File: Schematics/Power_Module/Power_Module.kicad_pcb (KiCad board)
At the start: 4 copper layers, 69.5 x 60 mm, 50 parts, among them J1 ScrewSwitch A, J2 ScrewSwitch B, J3 Battery B, J5 Battery A, J6 Stack Male Edge Connector, Q1 AO4447A, Q2 AO4447A, U1 LMR51430XDDCR, U2 LMR51430XDDCR, U3 LMR51430XDDCR

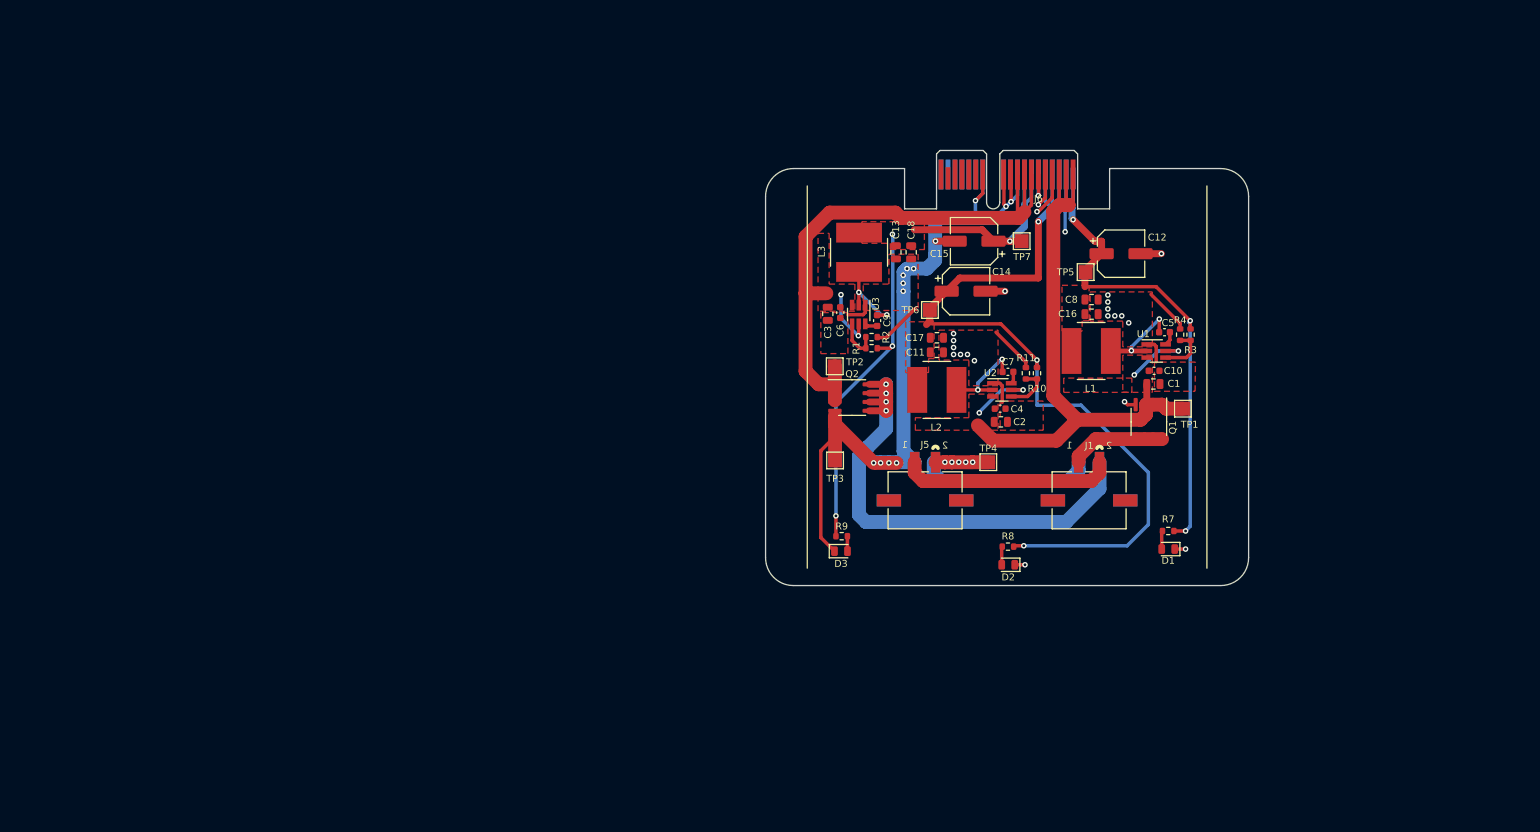
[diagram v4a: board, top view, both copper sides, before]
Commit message: Added part numbers, finalized PCB layout
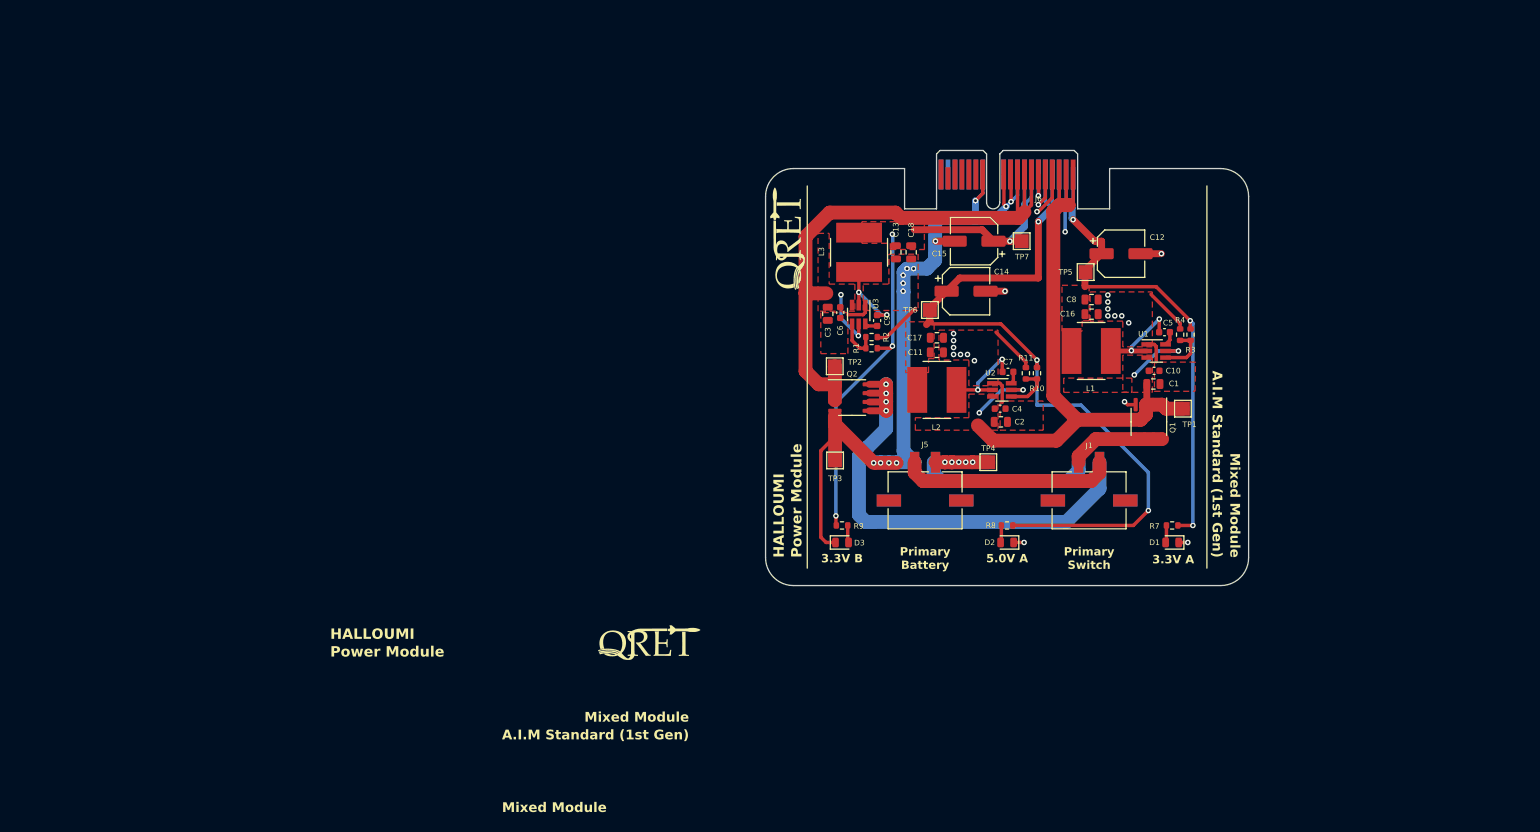
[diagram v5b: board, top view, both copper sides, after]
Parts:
- moved D2 3.21 mm to (165.0, 93.5)
- moved R8 3.05 mm to (165.0, 91.1)
- moved R9 1.55 mm to (141.2, 91.1)
- moved D3 1.26 mm to (141.2, 93.5)
- moved D1 1.11 mm to (188.8, 93.5)
- moved R7 0.98 mm to (188.8, 91.1)
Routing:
- net 5.0V_A: track 114.1 -> 111.8 mm
- net 3.3V_B: track 80.1 -> 78.5 mm
- net GND2: track 127.8 -> 129.0 mm
- net 3.3V_A: track 75.0 -> 74.2 mm
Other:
- board text added: "3.3V A"
- board text added: "3.3V B"
- board text added: "5.0V A"
- board text added: "A.I.M Standard (1st Gen)"
- board text added: "HALLOUMI"
- board text added: "Halloumi Rev 1.0 QRET Mar 2024 Rajan Laird Kennan Bays Oak Campbell"
- board text added: "Mixed Module"
- board text added: "Power Module"
- board text added: "Primary Battery"
- board text added: "Primary Switch"
- board text added: "Secondary Battery"
- board text added: "Secondary Switch"
- board text removed: "PLACE POWER CONNECTORS HERE (okay if on bottom)"

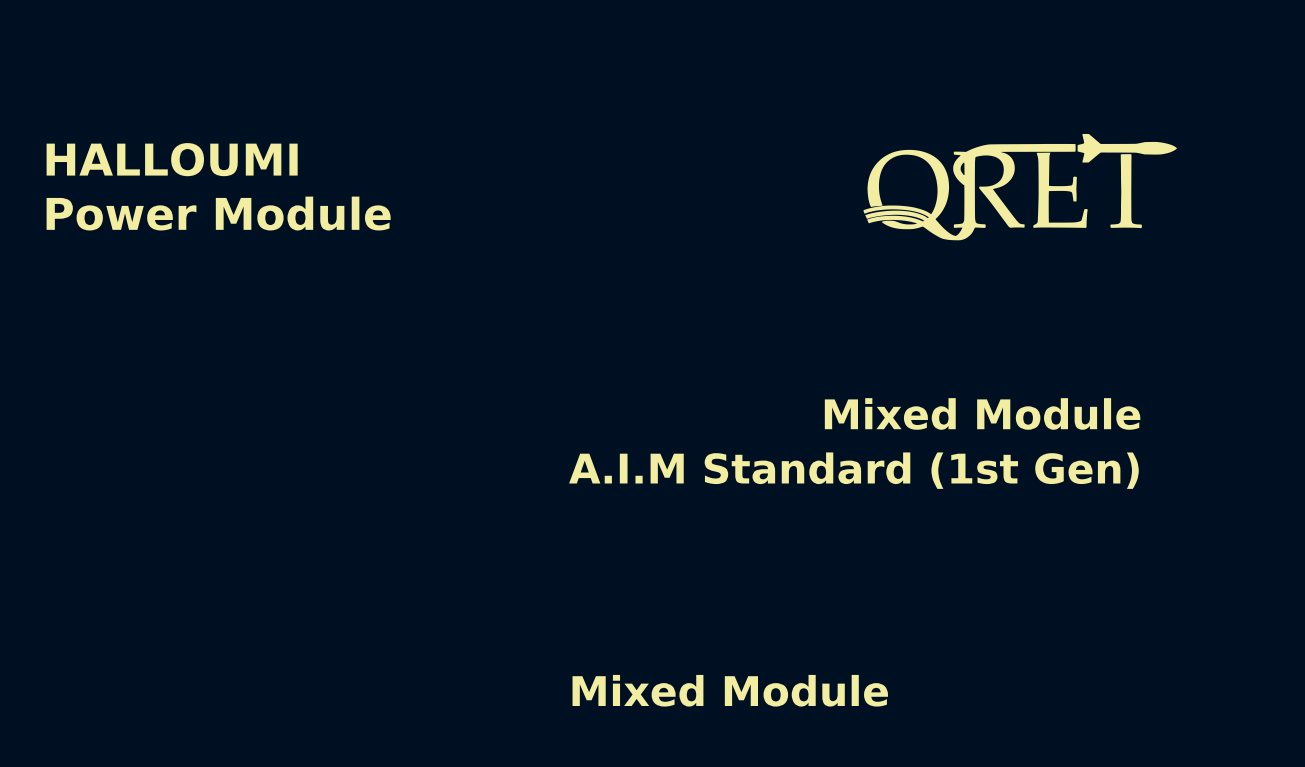
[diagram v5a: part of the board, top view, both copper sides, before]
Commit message: Minor Adjustments
- Adjusted LED resistor values
- Cleaned up PCB project lightly
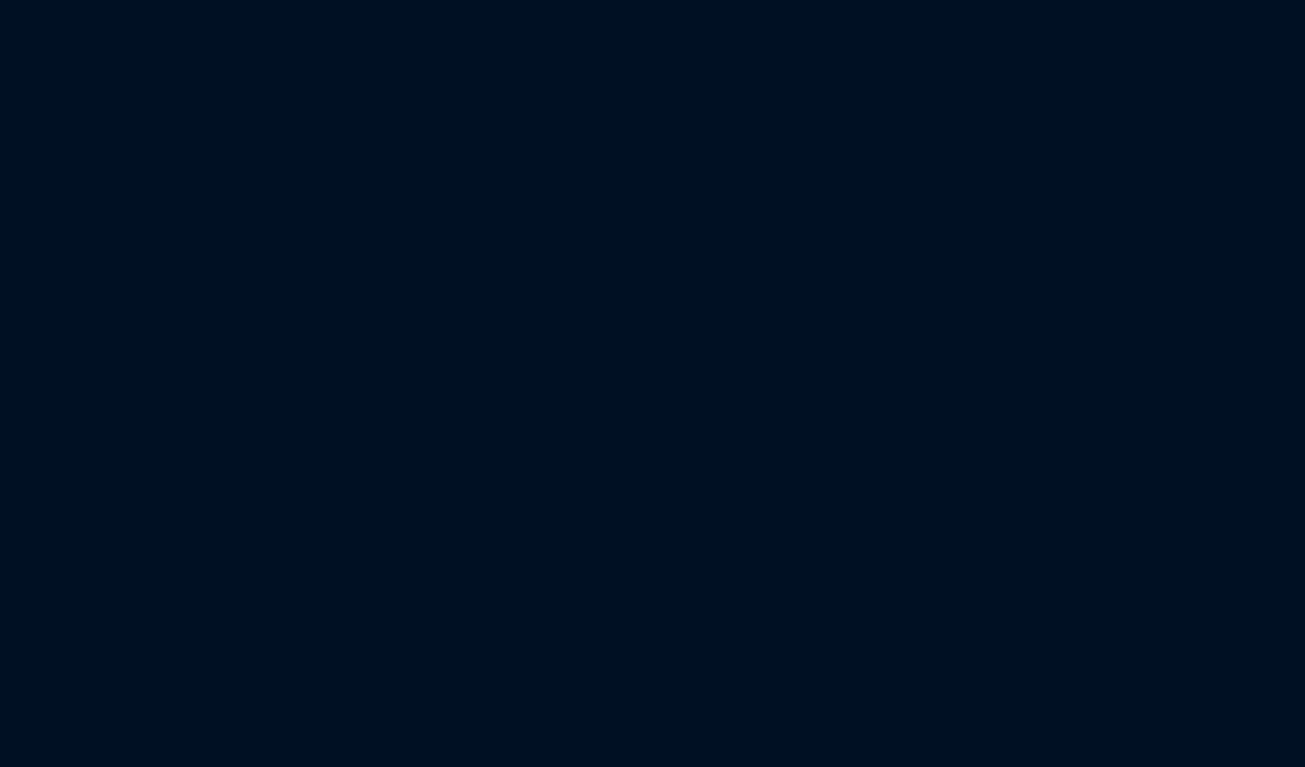
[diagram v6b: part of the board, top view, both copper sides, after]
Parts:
- R7, R9: value 510R -> 1.2k
- R8: value 2k -> 2.4k
